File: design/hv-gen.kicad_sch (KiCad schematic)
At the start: 23 parts, among them Q1 Q_NMOS_DGS, Q3 PNP, T2 DA2033-AL, U5 TLP152TPL_E

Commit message: _
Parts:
- R9: value R -> 1

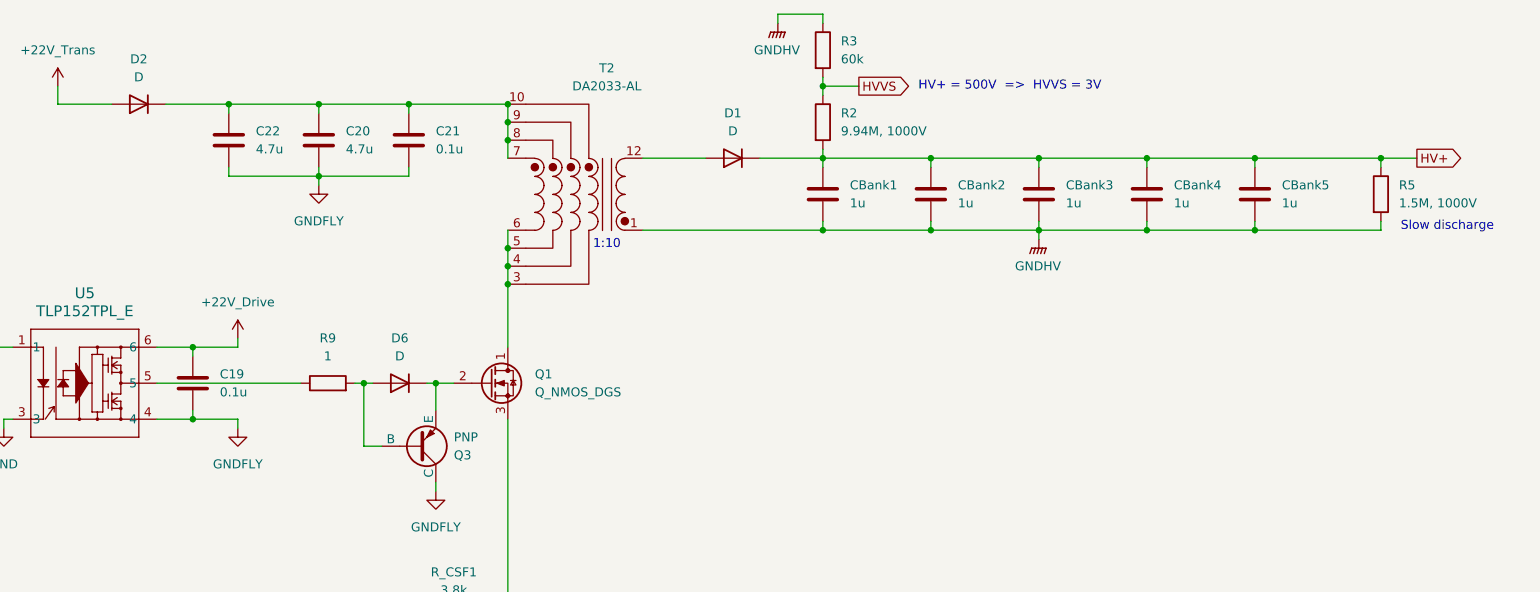
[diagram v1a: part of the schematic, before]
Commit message: Working on probe voltage and current sense circuits
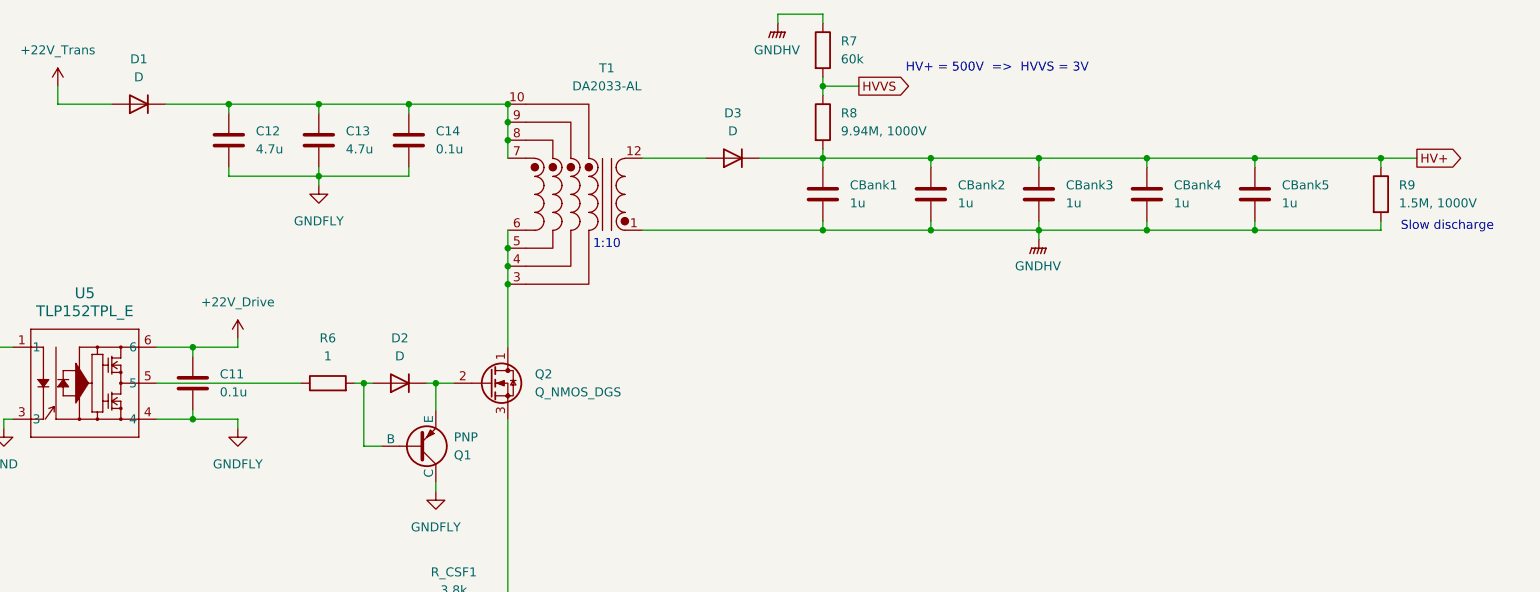
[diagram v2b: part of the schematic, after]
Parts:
- renumbered C19 to C11, C22 to C12, C20 to C13, C21 to C14, D2 to D1, D6 to D2, D1 to D3, Q3 to Q1, Q1 to Q2, R9 to R6, R3 to R7, R2 to R8, R5 to R9, T2 to T1

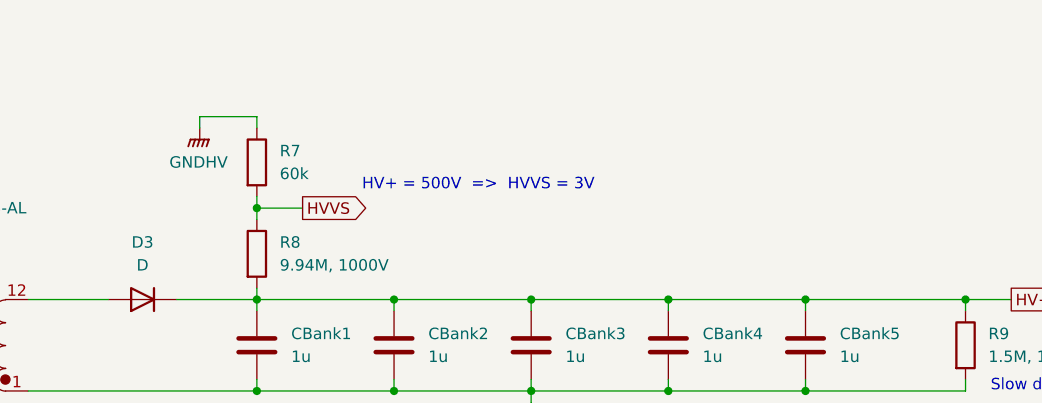
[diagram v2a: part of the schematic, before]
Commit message: Added low pass filter to high voltage sensing circuit
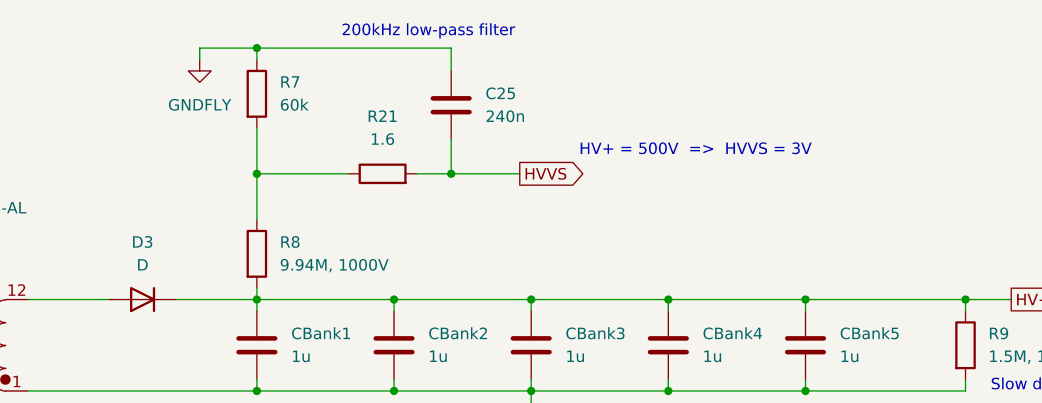
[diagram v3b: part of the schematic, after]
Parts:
- added C25: 240n, symbol Device:C
- added R21: 1.6, symbol Device:R
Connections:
- net GNDFLY: now also R7.1, C25.1
- net GNDHV: no longer R7.1
- net HVVS: now also C25.2, R21.2; no longer R7.2, R8.1
- new net: R21.1, R7.2, R8.1
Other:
- note added: "200kHz low-pass filter"
- moved on the sheet: R7

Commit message: organizing
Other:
- note added: "Current Sense"
- note added: "Flyback Plant"
- note added: "High Voltage Bank"
- note added: "Voltage Sense"
- moved on the sheet: C11, C12, C13, C14, C25, CBank1, CBank2, CBank3, CBank4, CBank5, C_CSF1, D1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

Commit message: Primary power buck regulator
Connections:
- net +22V_Trans is gone; now on net +22V: D1.2 (A)
- net +22V_Drive renamed +22V

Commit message: Working on measure buffers and assigning footprints
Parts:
- C11, C12, C13, C14, C25, C_CSF1: footprint (none) -> Capacitor_SMD:C_0402_1005Metric
- CBank1, CBank2, CBank3, CBank4, CBank5: footprint (none) -> Capacitor_SMD:C_0603_1608Metric
- R_CSF1: footprint (none) -> Resistor_SMD:R_0402_1005Metric
- U5: footprint TLP152_4P55X3P7_TOS -> project-footprints:TLP152_4P55X3P7_TOS

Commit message: _
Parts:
- added R24: 8.2M, symbol Device:R
- added R25: 1.8M, symbol Device:R
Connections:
- new net: R24.2, R25.1
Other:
- note added: "Use series resistor network to increase effective voltage rating. Helps avoid sourcing weird resistors"

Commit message: _
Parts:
- added R26, R27, R28: 2M, 150V, symbol Device:R
- R24: value 8.2M -> 2M, 150V
- R25: value 1.8M -> 2M, 150V
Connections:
- net at R24.1: now also R25.2
- net at R25.1: now also R27.2; no longer R24.2
- new net: R26.1, R28.2
- new net: R26.2, R27.1
